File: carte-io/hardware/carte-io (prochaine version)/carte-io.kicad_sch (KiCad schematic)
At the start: 0 parts

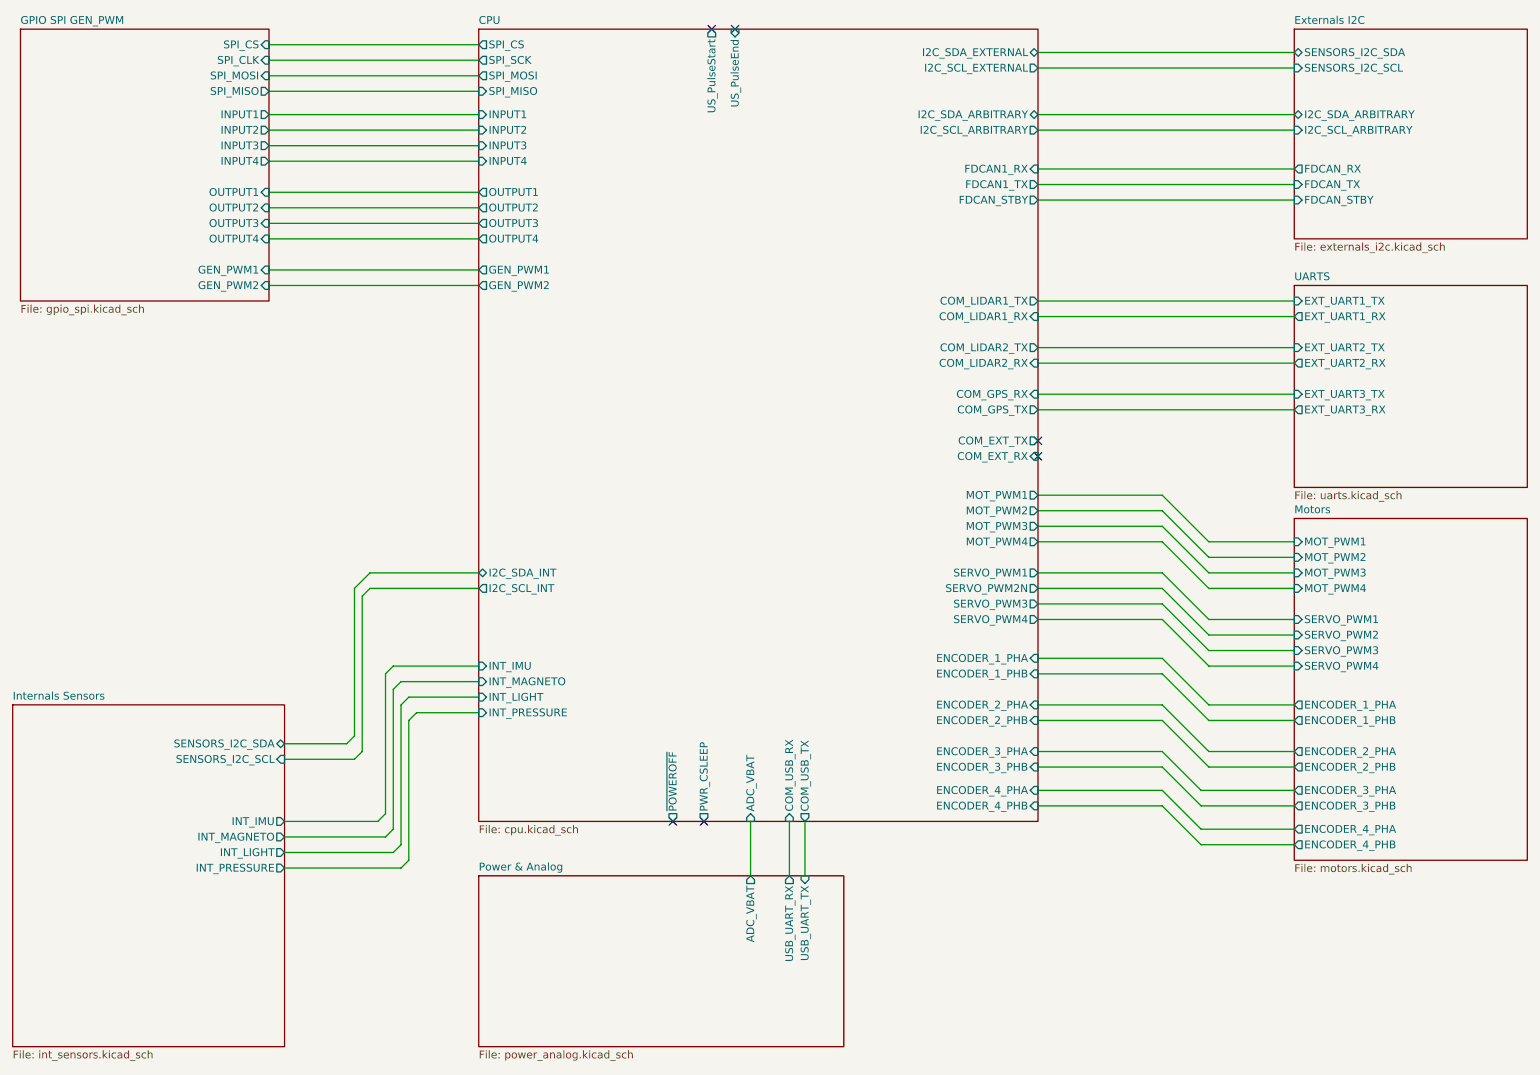
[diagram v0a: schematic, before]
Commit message: Commit de sauvegarde, gros changement sur la carte IO, les connecteurs sont compatibles SeeedStudio Grove. Il faut reprendre une grosse partie du routage et rajouter deux entrées analogiques
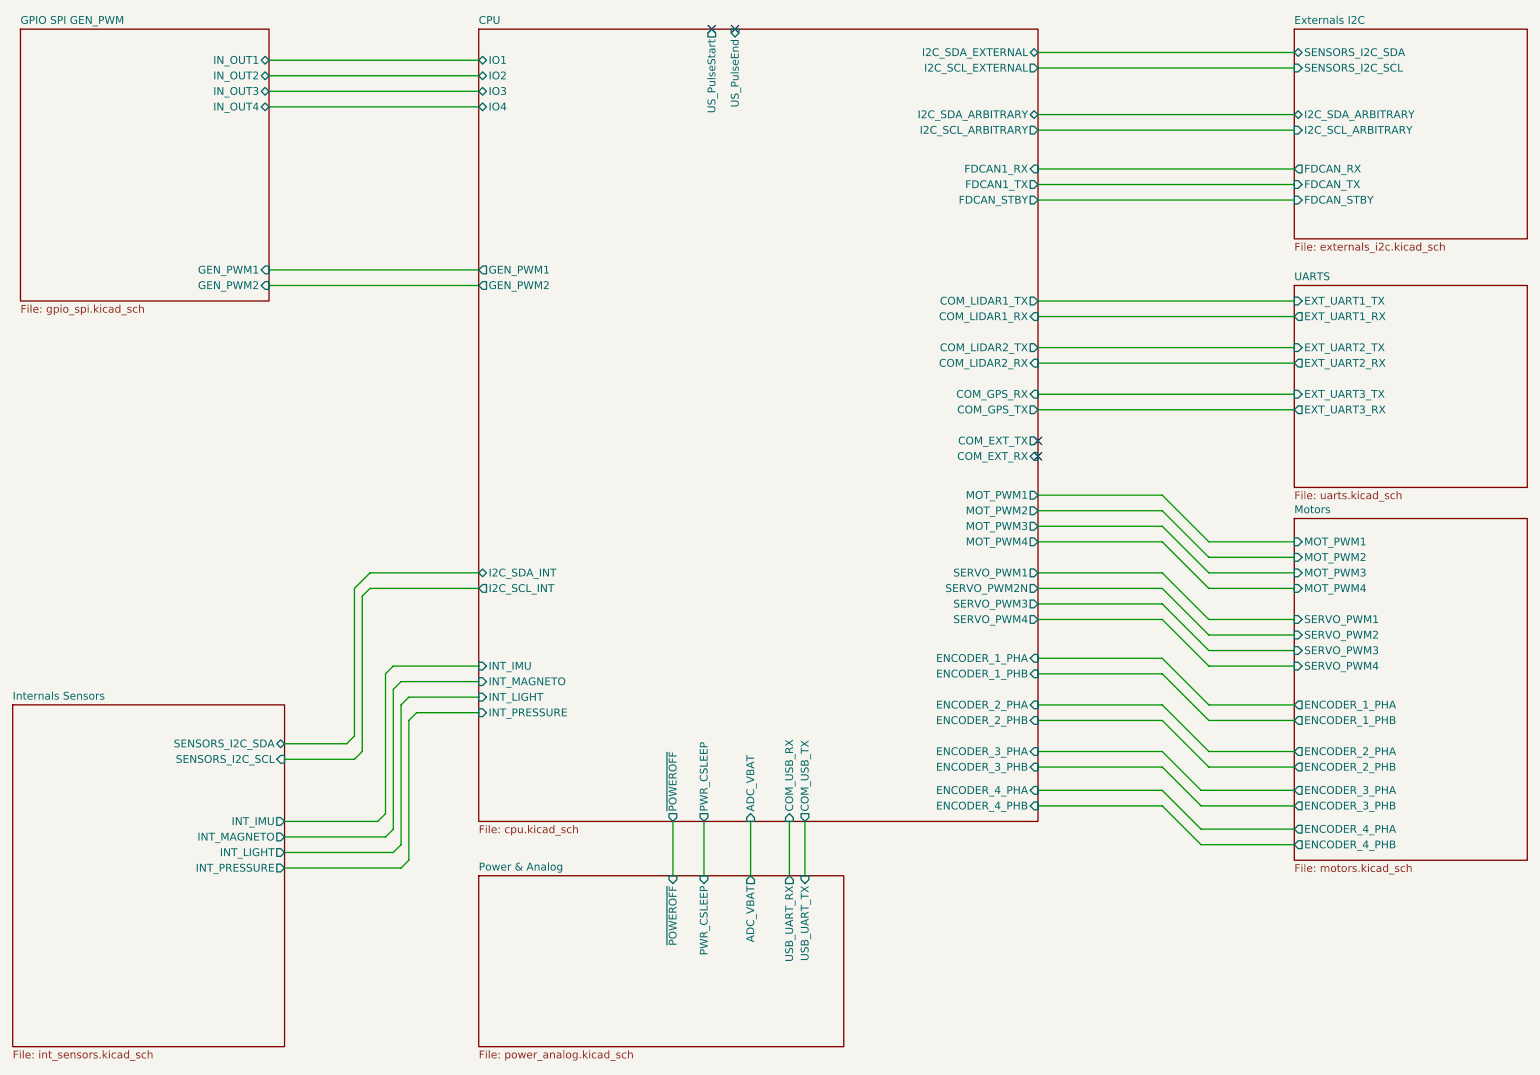
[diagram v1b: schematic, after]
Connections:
- no-connect marks 6 -> 4
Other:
- sheet CPU ports: added IO1, IO2, IO3, IO4; removed INPUT1, INPUT2, INPUT3, INPUT4, OUTPUT1, OUTPUT2, OUTPUT3, OUTPUT4, SPI_CS, SPI_MISO, SPI_MOSI, SPI_SCK
- sheet GPIO SPI GEN_PWM ports: added IN_OUT1, IN_OUT2, IN_OUT3, IN_OUT4; removed INPUT1, INPUT2, INPUT3, INPUT4, OUTPUT1, OUTPUT2, OUTPUT3, OUTPUT4, SPI_CLK, SPI_CS, SPI_MISO, SPI_MOSI
- sheet Power & Analog ports: added PWR_CSLEEP, ~{POWEROFF}; removed none

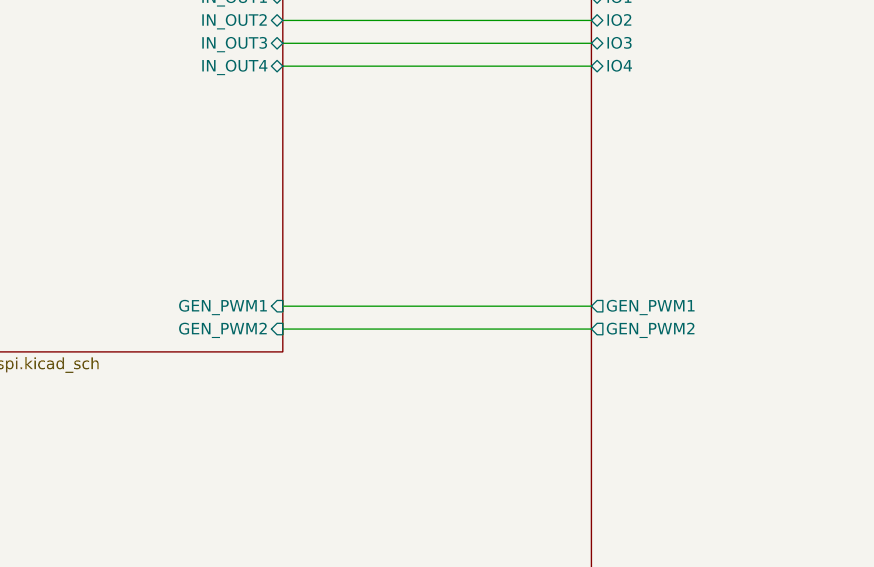
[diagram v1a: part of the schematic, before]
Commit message: -- reorganisation de la carte, - rajout des connecteurs seeedstudio grove - Rajout des deux entrées ADC
travail en cours
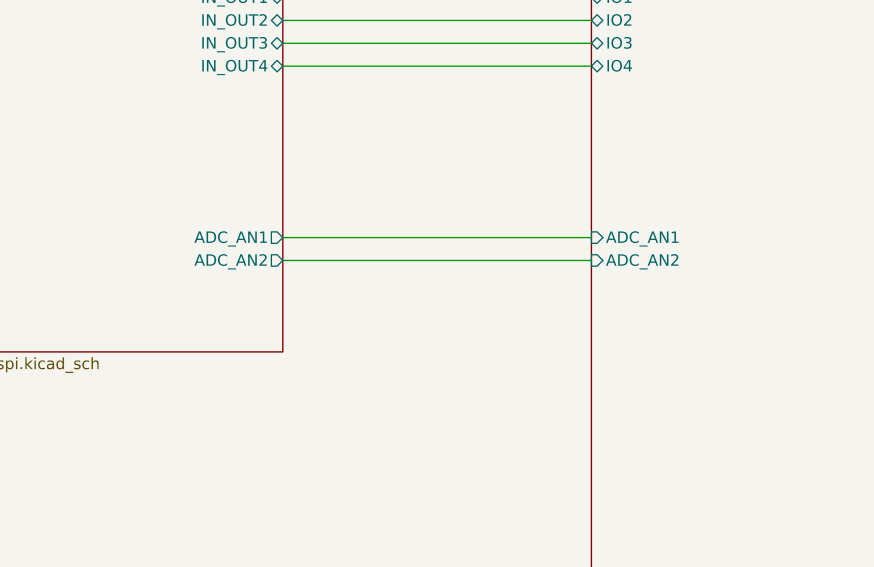
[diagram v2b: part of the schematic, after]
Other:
- sheet CPU ports: added ADC_AN1, ADC_AN2; removed GEN_PWM1, GEN_PWM2
- sheet GPIO SPI GEN_PWM ports: added ADC_AN1, ADC_AN2; removed GEN_PWM1, GEN_PWM2
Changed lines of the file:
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@@
-	(wire
-		(pts
-			(xy 68.58 64.77) (xy 102.87 64.77)
-		)
-		(stroke
-			(width 0)
-			(type default)
-		)
-	)
 	(wire
 		(pts
@@
 	(wire
 		(pts
-			(xy 68.58 62.23) (xy 102.87 62.23)
-		)
-		(stroke
-			(width 0)
-			(type default)
-		)
-	)
-	(wire
-		(pts
 			(xy 139.7 152.4) (xy 139.7 161.29)
 		)
@@
 	(wire
 		(pts
+			(xy 68.58 54.61) (xy 102.87 54.61)
+		)
+		(stroke
+			(width 0)
+			(type default)
+		)
+	)
+	(wire
+		(pts
 			(xy 82.55 138.43) (xy 82.55 114.3)
 		)
@@
 		(pts
 			(xy 222.25 124.46) (xy 236.22 124.46)
+		)
+		(stroke
+			(width 0)
+			(type default)
+		)
+	)
+	(wire
+		(pts
+			(xy 68.58 57.15) (xy 102.87 57.15)
 		)
 		(stroke
@@
 			)
 		)
-		(pin "GEN_PWM1" input
-			(at 68.58 62.23 0)
-			(effects
-				(font
-					(size 1.27 1.27)
-				)
-				(justify right)
-			)
-		)
-		(pin "GEN_PWM2" input
-			(at 68.58 64.77 0)
-			(effects
-				(font
-					(size 1.27 1.27)
-				)
-				(justify right)
-			)
-		)
 		(pin "IN_OUT1" bidirectional
 			(at 68.58 27.94 0)
@@
 		(pin "IN_OUT4" bidirectional
 			(at 68.58 35.56 0)
+			(effects
+				(font
+					(size 1.27 1.27)
+				)
+				(justify right)
+			)
+		)
+		(pin "ADC_AN2" output
+			(at 68.58 57.15 0)
+			(effects
+				(font
+					(size 1.27 1.27)
+				)
+				(justify right)
+			)
+		)
+		(pin "ADC_AN1" output
+			(at 68.58 54.61 0)
 			(effects
 				(font
@@
 			)
 		)
-		(pin "GEN_PWM2" output
-			(at 102.87 64.77 180)
-			(effects
-				(font
-					(size 1.27 1.27)
-				)
-				(justify left)
-			)
-		)
 		(pin "ENCODER_1_PHA" input
 			(at 194.31 125.73 0)
@@
 			)
 		)
-		(pin "GEN_PWM1" output
-			(at 102.87 62.23 180)
-			(effects
-				(font
-					(size 1.27 1.27)
-				)
-				(justify left)
-			)
-		)
 		(pin "PWR_CSLEEP" output
 			(at 139.7 152.4 270)
@@
 			(effects
 				(font
+					(size 1.27 1.27)
+				)
+				(justify left)
+			)
+		)
+		(pin "ADC_AN1" input
+			(at 102.87 54.61 180)
+			(effects
+				(font
+					(size 1.27 1.27)
+				)
+				(justify left)
+			)
+		)
+		(pin "ADC_AN2" input
+			(at 102.87 57.15 180)
+			(effects
+				(font

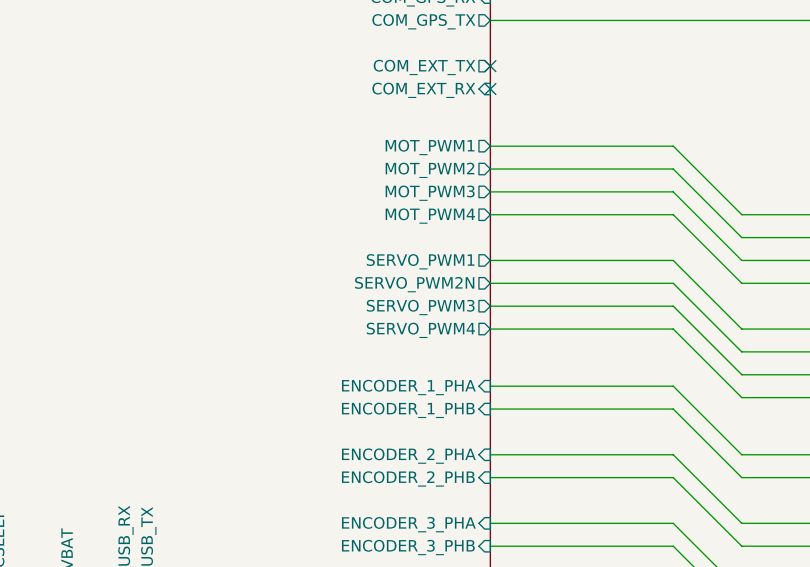
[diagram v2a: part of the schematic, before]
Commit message: WIP ajout du driver uart (marche) et du driver I2C (juste generé par chatgpt, à reprendre et tester)
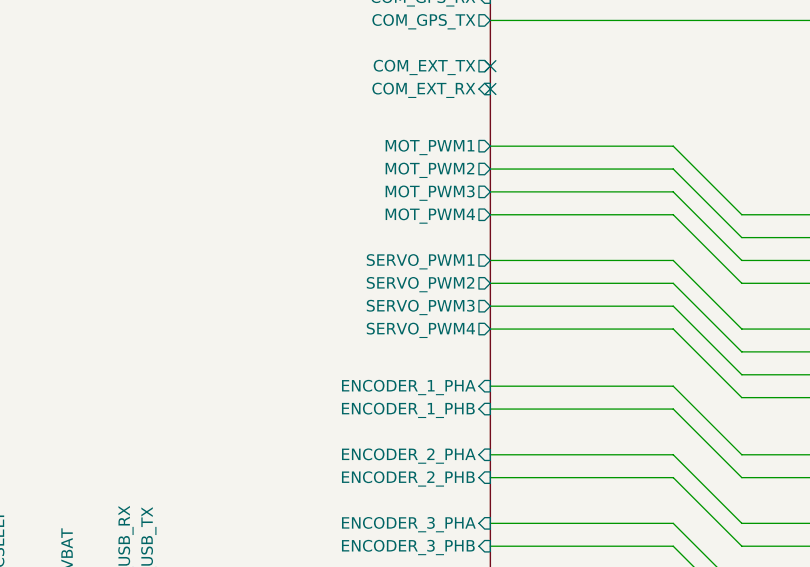
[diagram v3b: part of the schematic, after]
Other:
- sheet CPU ports: added SERVO_PWM2; removed SERVO_PWM2N
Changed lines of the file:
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@@
 			)
 		)
-		(pin "SERVO_PWM2N" output
+		(pin "SERVO_PWM2" output
 			(at 194.31 114.3 0)
 			(effects
